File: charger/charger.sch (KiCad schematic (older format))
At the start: 105 parts, among them J1 OSTT7020150, J2 Conn_01x06, J3 Conn_01x06, J4 Conn_01x03, J5 OSTT7020150, Q1 CSD18540Q5B, Q2 CSD19531Q5A, Q3 CSD19531Q5A, Q4 CSD19531Q5A, Q5 CSD19531Q5A, Q6 CSD18540Q5B, U1 MSP432, U2 NCP718xSN500, U3 UCC27517DBVR, U4 INA240A2PW, U5 LM5109BMA, U6 LM5109BMA, U7 INA240A2PW, U8 LM5009MM, U9 AP131-33

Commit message: finished pcb
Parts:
- R24: footprint Resistor_SMD:R_1206_3216Metric -> Resistor_SMD:R_2512_6332Metric
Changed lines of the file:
@@
 F 0 "R24" V 8045 2500 50  0000 C CNN
 F 1 "0.002" V 8136 2500 50  0000 C CNN
-F 2 "Resistor_SMD:R_1206_3216Metric" V 8290 2490 50  0001 C CNN
-F 3 "~" H 8250 2500 50  0001 C CNN
+F 2 "Resistor_SMD:R_2512_6332Metric" V 8290 2490 50  0001 C CNN
+F 3 "https://www.mouser.com/ProductDetail/Yageo/PU2512FKMP50R002L?qs=sGAEpiMZZMvdGkrng054t0c0U24Fa%2Fv2NfStLNxNcuIQTzdklHgYjw%3D%3D" H 8250 2500 50  0001 C CNN
 	1    8250 2500
 	0    1    1    0

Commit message: charger pcb v2
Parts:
- removed C12, C13: 560 uF, Capacitor_SMD:C_1206_3216Metric, symbol Device:C
- removed C14, C15: 220 uF, Capacitor_SMD:C_1206_3216Metric, symbol Device:C
- removed C30, C32: 1 uF, Capacitor_SMD:C_1206_3216Metric, symbol Device:C
- removed C33: 22 nF, Capacitor_SMD:C_1206_3216Metric, symbol Device:C
- removed C35: 10 uF, Capacitor_SMD:C_1206_3216Metric, symbol Device:C
- removed D6: B1100B, Diode_SMD:D_SMB, symbol Device:D_Schottky
- removed J1: OSTT7020150, Connector_PinHeader_2.54mm:PinHeader_1x06_P2.54mm_Vertical, symbol Connector:Screw_Terminal_01x06
- removed J2, J3: Conn_01x06, Connector_PinHeader_2.54mm:PinHeader_1x06_P2.54mm_Vertical, symbol Connector_Generic:Conn_01x06
- removed J4: Conn_01x03, Connector_PinHeader_2.54mm:PinHeader_1x03_P2.54mm_Vertical, symbol Connector_Generic:Conn_01x03
- removed L3: 220 uH, Inductor_SMD:L_Bourns_SRR1260, symbol Device:L
- removed R2: 1k, Resistor_SMD:R_1206_3216Metric, symbol Device:R_US
- removed R25: 430k, Resistor_SMD:R_1206_3216Metric, symbol Device:R_Small_US
- removed R26: 169k, Resistor_SMD:R_1206_3216Metric, symbol Device:R_Small_US
- removed R27, R28: 0 ohm, Resistor_SMD:R_1206_3216Metric, symbol Device:R_Small_US
- removed R29: 3k, Resistor_SMD:R_1206_3216Metric, symbol Device:R_Small_US
- removed R30: 1k, Resistor_SMD:R_1206_3216Metric, symbol Device:R_Small_US
- removed R31: 3, Resistor_SMD:R_1206_3216Metric, symbol Device:R_Small_US
- removed U1: MSP432, MWD_Footprints:MSP432, symbol MSP_mwd:MSP432
- removed U8: LM5009MM, Package_SO:MSOP-8_3x3mm_P0.65mm, symbol Regulator_Switching:LM5009MM
- added C11, C12: 560u, Capacitor_SMD:C_Elec_8x10.2, symbol Device:CP
- added C13, C14: 220u, Capacitor_SMD:C_Elec_6.3x7.7, symbol Device:CP
- added C21, C22, C31: 0.1 uF, Capacitor_SMD:C_1206_3216Metric, symbol Device:C
- added C30: 68u, Capacitor_SMD:C_Elec_8x10.2, symbol Device:CP
- added C37: 120u, Capacitor_SMD:C_Elec_10x10.2, symbol Device:CP
- added D6: MBRS140T3G, Diode_SMD:D_SMB_Handsoldering, symbol Diode:1N5819
- added J1: OSTT7020150, MWD_Footprints:Phoenix_MKDS_6.35, symbol Connector:Screw_Terminal_01x02
- added J3: MECF-50-01-X-DV, SAMTEC_MECF-50-01-X-DV, symbol MECF-50-01-X-DV:MECF-50-01-X-DV
- added L3: 330 uH, Inductor_SMD:L_Bourns_SRR1260, symbol pspice:INDUCTOR
- added R25, R26: 47k, Resistor_SMD:R_1206_3216Metric, symbol Device:R_US
- added U6, U7: LM321, Package_TO_SOT_SMD:SOT-23-5, symbol Amplifier_Operational:LM321
- added U9: LM2594HVM-12, Package_SO:SOIC-8_3.9x4.9mm_P1.27mm, symbol Regulator_Switching:LM2594HVM-12
- J2: renamed from J5; footprint Connector_PinHeader_2.54mm:PinHeader_1x02_P2.54mm_Vertical -> MWD_Footprints:Phoenix_MKDS_6.35
- R10: renamed from R5; value 950k -> 698k
- R12: renamed from R18; value 1M -> 806k
- R3: footprint Resistor_SMD:R_1206_3216Metric -> Resistor_SMD:R_2512_6332Metric
- U3: renamed from U4; footprint Package_SO:TSSOP-8_4.4x3mm_P0.65mm -> Package_SO:SOIC-8_3.9x4.9mm_P1.27mm
- U8: renamed from U7; footprint Package_SO:TSSOP-8_4.4x3mm_P0.65mm -> Package_SO:SOIC-8_3.9x4.9mm_P1.27mm
- renumbered C3 to C1, C11 to C10, C16 to C15, C17 to C16, C8 to C17, C22 to C18, C4 to C2, C27 to C26, C29 to C27, C26 to C28, C28 to C29, C5 to C3, C31 to C32, C1 to C33, C2 to C35, C6 to C4, C7 to C5, C18 to C6, C9 to C7, C10 to C8, C21 to C9, R6 to R11, R19 to R13, R12 to R14, R13 to R15, R14 to R16, R15 to R17, R16 to R18, R17 to R19, R23 to R22, R22 to R23, R11 to R5, R7 to R6, R8 to R7, R9 to R8, R10 to R9, U3 to U1, U2 to U10, U9 to U11, U5 to U4, U6 to U5
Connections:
- net +10V is gone; now on net +12V: C1.2, C15.2, C16.2, C33.1, D1.2 (A), D2.2 (A), TP5.1, U1.1, U10.1 (IN), U4.1 (VDD), U5.1 (VDD)
- net +3V3: now also J3.1 (01), J3.11, J3.13, J3.15, J3.3 (03), J3.5 (05), J3.7 (07), J3.9 (09), U6.5 (V+), U7.5 (V+)
- net +5V: now also U11.3 (EN)
- net G1_H: now also J3.27
- net G1_L: now also J3.25
- net G2_H: now also J3.31
- net G2_L: now also J3.29
- net GND: now also C11.2, C12.2, C13.2, C14.2, C21.2, C22.2, C30.2, C37.2, D6.2 (A), J3.18, J3.20, J3.22, J3.24, J3.26, J3.28, J3.30, J3.32, R26.1, U6.2 (V-), U7.2 (V-), U9.6 (GND)
- net I_bat_sense: now also J3.59
- net I_in_sense: now also J3.53
- net Input_EN: now also J3.72
- net PWM_H1: now also C13.1
- net PWM_H2: now also C14.1
- net PWM_L1: now also C11.1
- net PWM_L2: now also C12.1
- net V_bat_sense: now also C22.1, J3.57, U7.3 (-), U7.4; no longer C18.1, R12.2, R13.1
- net V_in: now also C30.1, C31.1, U9.7 (VIN)
- net V_in_sense: now also C21.1, J3.49, U6.3 (-), U6.4; no longer C17.1, R10.2, R11.1
- net V_out: now also L1.1; no longer L1.2
- net V_solar: now also J1.2 (Pin_2)
- net V_solar-: now also J1.1 (Pin_1)
- net +12V: now reaches U10.3 (EN)
- net +12V: now also C37.1, L3.2, U9.4 (FB)
- net at Q2.1 (S), Q2.2 (S), Q2.3 (S)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: now also L1.2; no longer L1.1
- new net: C17.1, R10.2, R11.1, U6.1 (+)
- new net: C18.1, R12.2, R13.1, U7.1 (+)
- new net: R25.1, R26.2, U9.5 (~ON~/OFF)
- new net: D6.1 (K), L3.1, U9.8 (OUT)
- new net: C31.2, R25.2
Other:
- moved on the sheet: C17, C18, C26, C27, C32, C33, C34, C35, C36, C6, C9, D5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

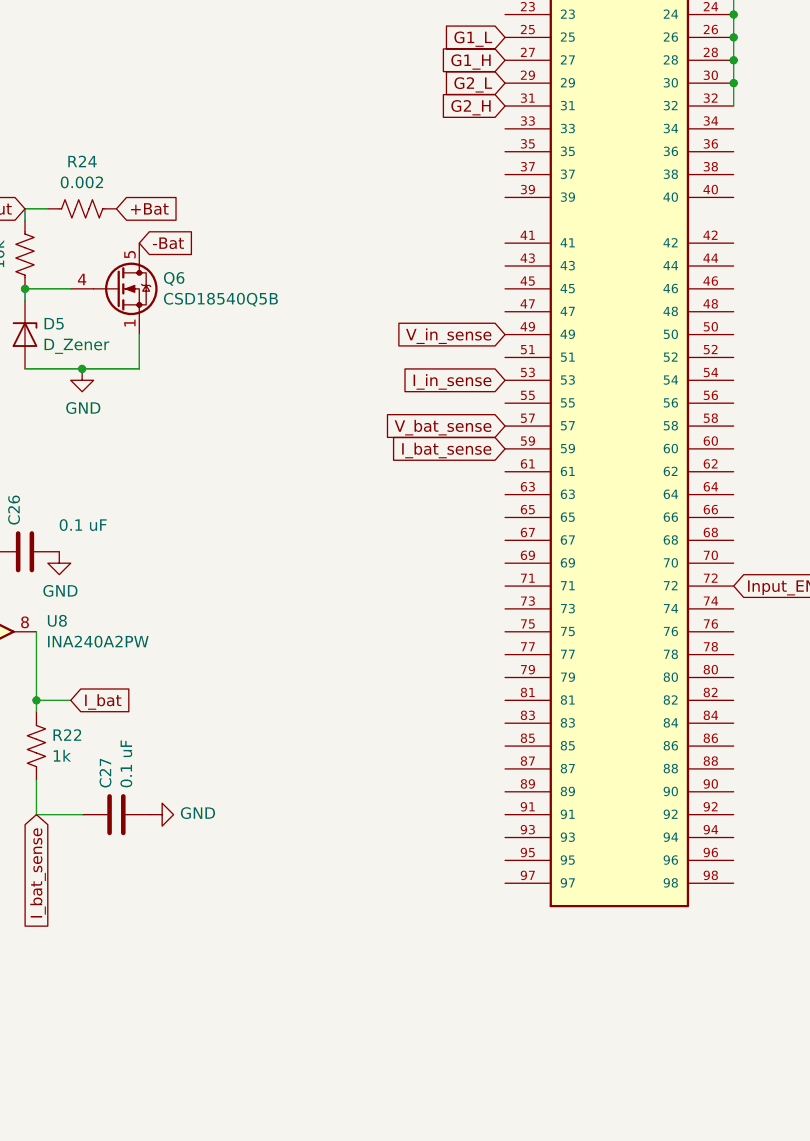
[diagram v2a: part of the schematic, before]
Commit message: update gitignore
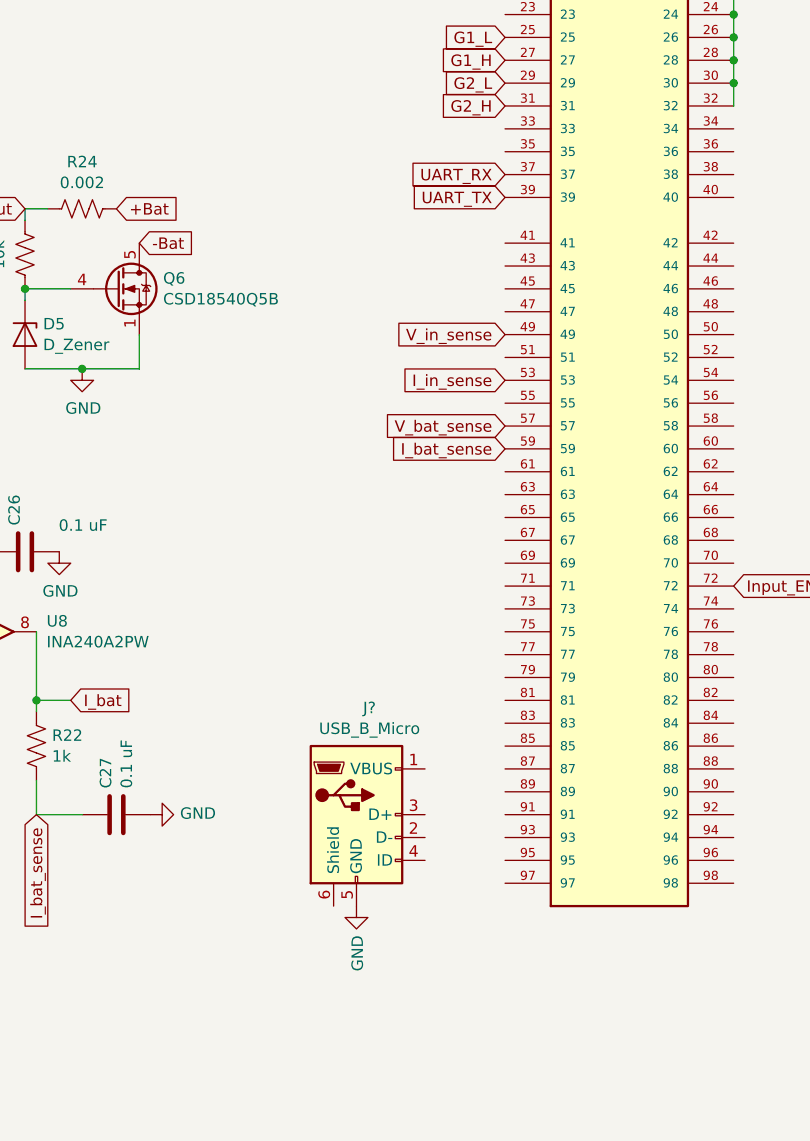
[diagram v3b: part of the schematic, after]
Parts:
- added J?: USB_B_Micro, symbol Connector:USB_B_Micro
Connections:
- net GND: now also J?.5 (GND)
- net UART_RX: now reaches J3.37
- net UART_TX: now reaches J3.39
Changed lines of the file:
@@
+	1    0    0    -1
+$EndComp
+Text GLabel 9550 3050 0    50   Input ~ 0
+UART_TX
+Text GLabel 9550 2950 0    50   Input ~ 0
+UART_RX
+$Comp
+L Connector:USB_B_Micro J?
+U 1 1 5FCC8E20
+P 8900 5750
+F 0 "J?" H 8957 6217 50  0000 C CNN
+F 1 "USB_B_Micro" H 8957 6126 50  0000 C CNN
+F 2 "" H 9050 5700 50  0001 C CNN
+F 3 "~" H 9050 5700 50  0001 C CNN
+	1    8900 5750
+	1    0    0    -1
+$EndComp
+$Comp
+L power:GND #PWR?
+U 1 1 5FCDB6D6
+P 8900 6150
+F 0 "#PWR?" H 8900 5900 50  0001 C CNN
+F 1 "GND" V 8905 6022 50  0000 R CNN
+F 2 "" H 8900 6150 50  0001 C CNN
+F 3 "" H 8900 6150 50  0001 C CNN
+	1    8900 6150
 	1    0    0    -1
 $EndComp
